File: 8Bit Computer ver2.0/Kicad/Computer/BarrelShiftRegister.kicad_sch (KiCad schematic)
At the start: 14 parts, among them IC169 SN74LVC1G14DBVR, IC170 SN74LVC1G32DBVR, IC171 SN74AHC157DR, IC172 SN74AHC157DR, IC173 SN74AHC74DR, IC174 SN74LVC1G08DBVR, IC175 SN74AHC157DR, IC176 SN74AHC157DR, IC177 SN74LVC1G08DBVR, IC178 SN74LVC1G08DBVR, IC179 SN74AHC08DR, IC180 SN74AHC157DR, IC181 SN74AHC157DR, IC182 SN74ABT574ADWR

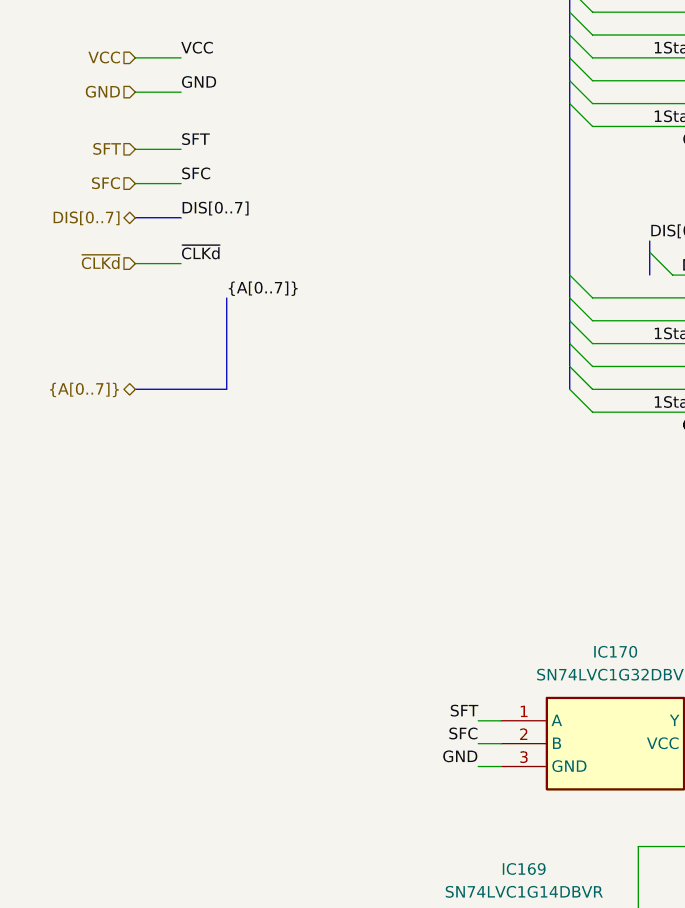
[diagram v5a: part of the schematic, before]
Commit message: Kicad Fixes only schematic
fixed important schematic errors
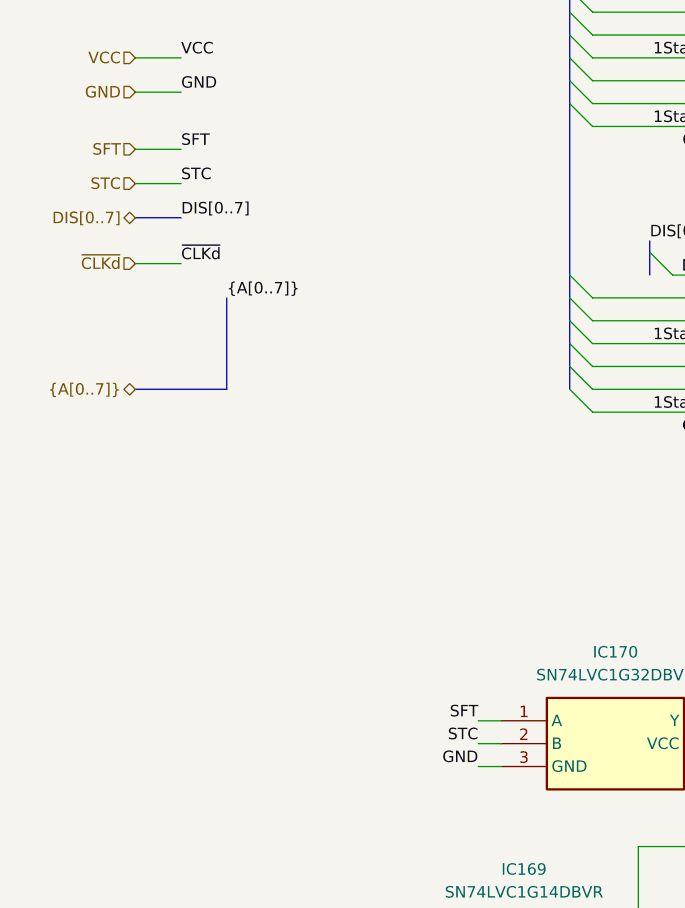
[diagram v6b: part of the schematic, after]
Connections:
- net SFC is gone; now on net STC: IC170.2 (B)
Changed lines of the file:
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@@
 		)
 	)
-	(label "SFC"
+	(label "STC"
 		(at 74.93 167.64 180)
 		(effects
@@
 		)
 	)
+	(label "STC"
+		(at 41.91 105.41 0)
+		(effects
+			(font
+				(size 1.27 1.27)
+			)
+			(justify left bottom)
+		)
+	)
 	(label "DAT4"
 		(at 400.05 124.46 0)
@@
 			)
 			(justify right bottom)
-		)
-	)
-	(label "SFC"
-		(at 41.91 105.41 0)
-		(effects
-			(font
-				(size 1.27 1.27)
-			)
-			(justify left bottom)
 		)
 	)
@@
 		)
 	)
-	(hierarchical_label "SFC"
+	(hierarchical_label "STC"
 		(shape input)
 		(at 36.83 105.41 180)

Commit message: part 1 of changing to A4
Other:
- moved on the sheet: IC169, IC170, IC171, IC172, IC173, IC174, IC175, IC176, IC177, IC178, IC179, IC180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
